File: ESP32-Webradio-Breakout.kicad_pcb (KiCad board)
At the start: 2 copper layers, 113.7 x 85.1 mm, 6 parts, among them J1 Conn_01x19, J2 Conn_01x19, SW1 RotaryEncoder_Switch

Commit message: adding RCA Jack Connector to board
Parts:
- added J3: RCJ-042, RCJ-042:CUI_RCJ-042, F.Cu at (212.9, 56.9)
- added J4: RCJ-041, RCJ-041:CUI_RCJ-041, F.Cu at (212.9, 71.2)

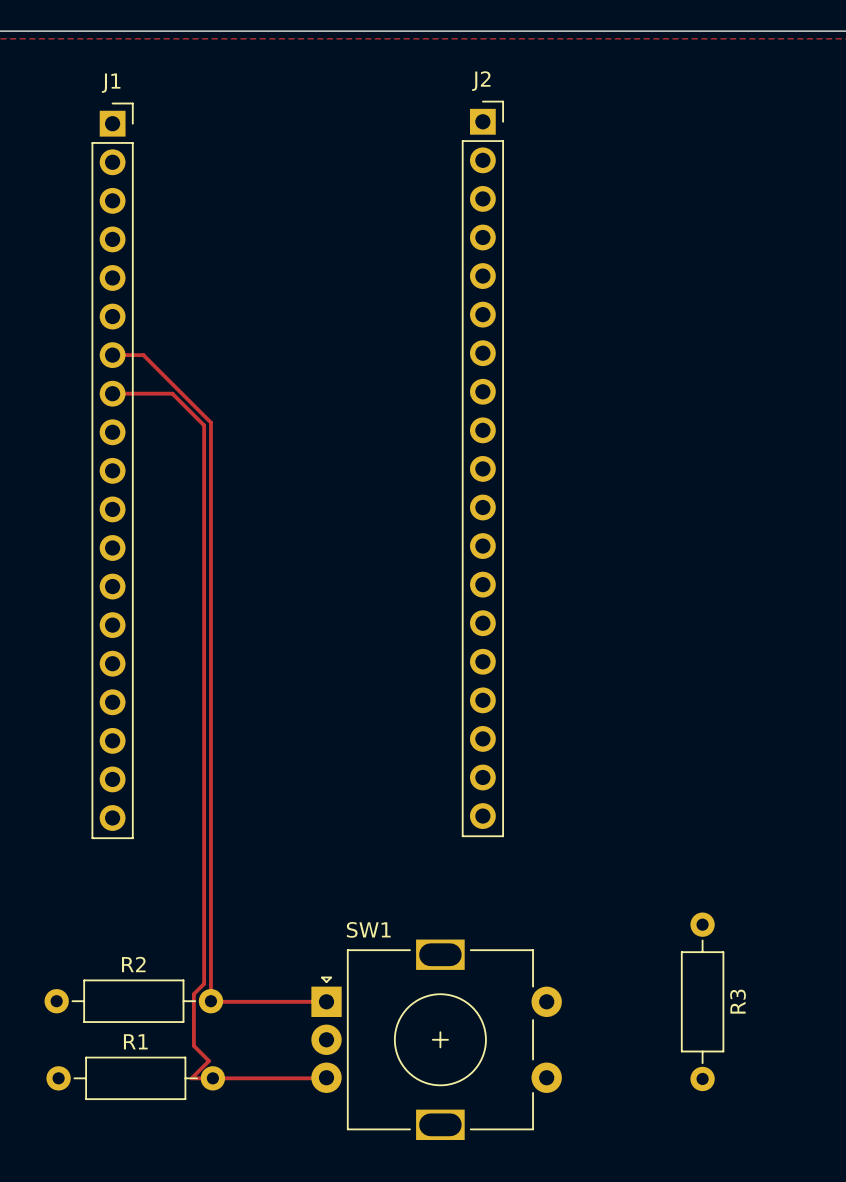
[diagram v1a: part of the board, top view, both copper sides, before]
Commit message: adding ESP32-NodeMCU to Project Lib
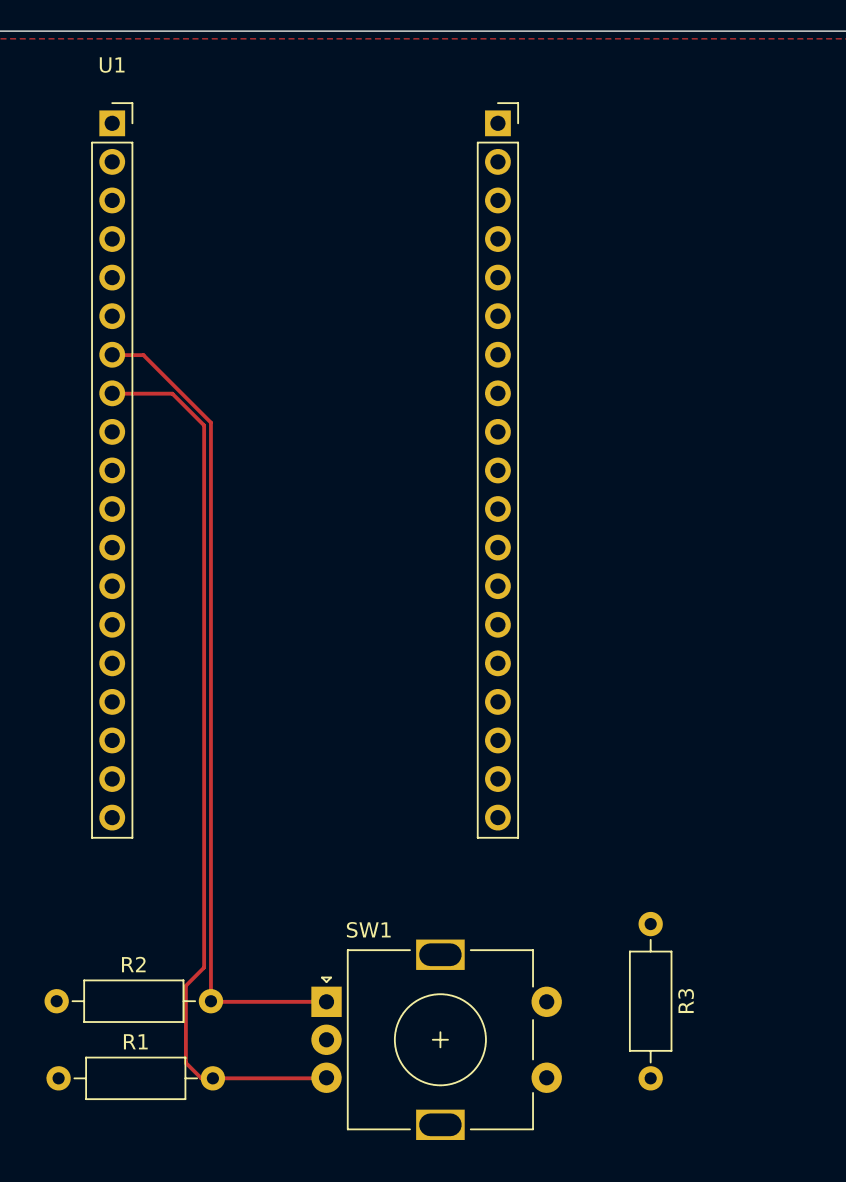
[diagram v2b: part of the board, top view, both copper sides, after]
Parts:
- removed J1, J2: Conn_01x19, Connector_PinSocket_2.54mm:PinSocket_1x19_P2.54mm_Vertical
- added U1: ESP32NodeMCU, ESP32-NodeMCU_WROOM_32:ESP32-NodeMCU_WROOM_32, F.Cu at (112.1, 43.0)
- moved R3 3.42 mm to (147.6, 95.8)
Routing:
- net /G33/Enc_B: track 59.9 -> 59.1 mm

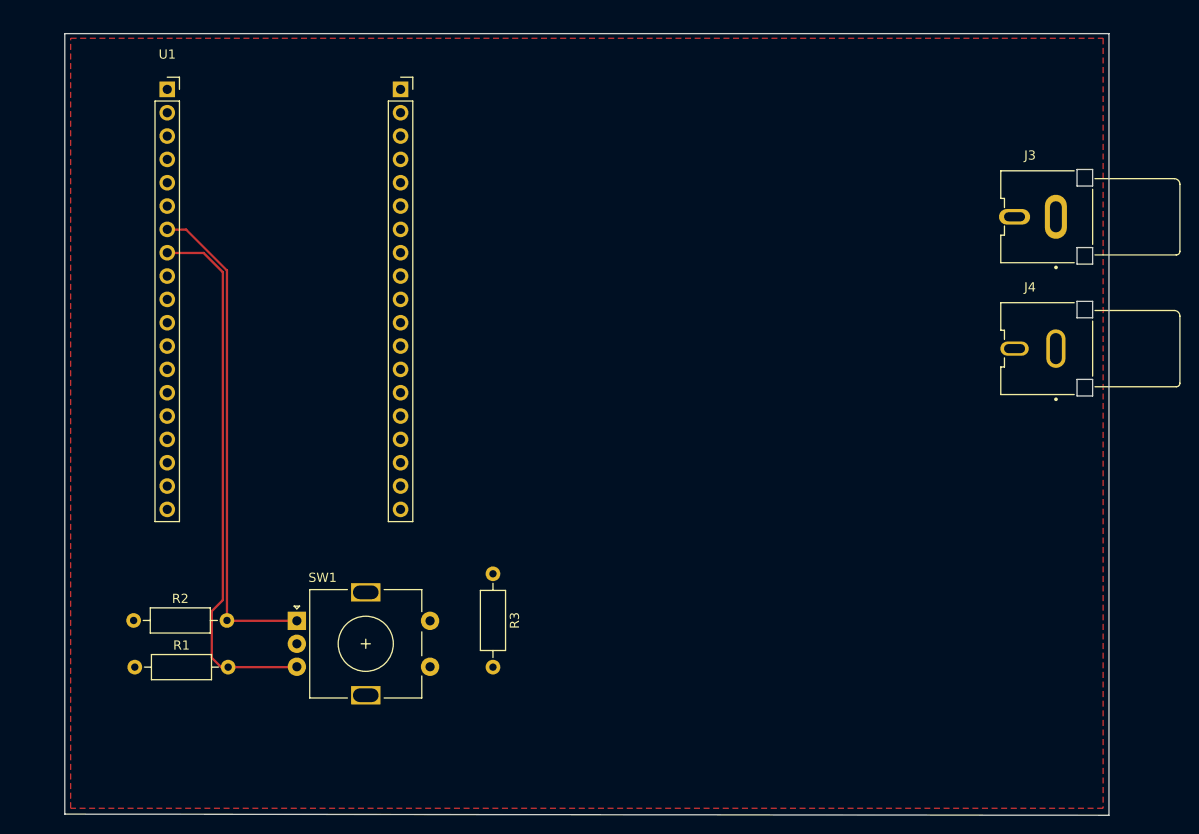
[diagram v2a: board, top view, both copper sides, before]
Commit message: adding CC BY-SA 4.0 licens to the Project
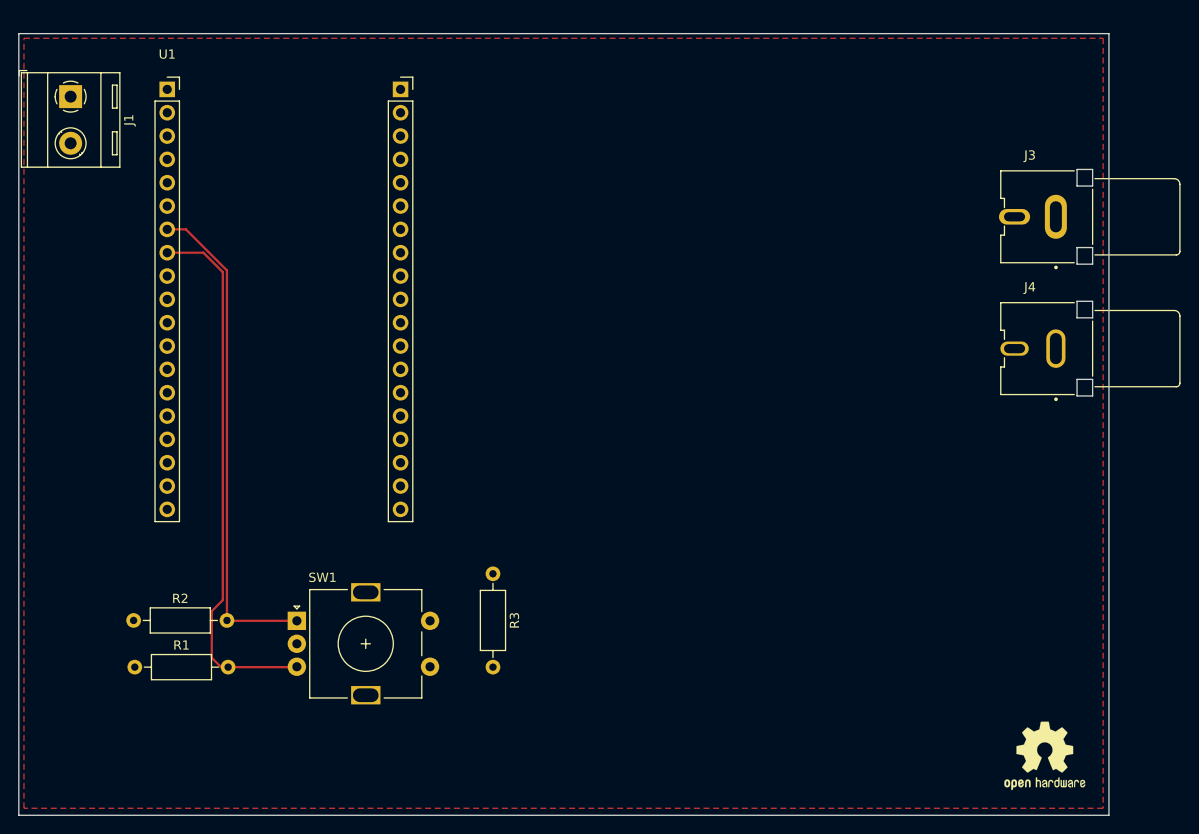
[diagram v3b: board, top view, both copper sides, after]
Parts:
- added J1: Conn_01x02, TerminalBlock_RND:TerminalBlock_RND_205-00287_1x02_P5.08mm_Horizontal, F.Cu at (101.6, 43.8)
- added REF**: OSHW-Logo2_9.8x8mm_SilkScreen, Symbol:OSHW-Logo2_9.8x8mm_SilkScreen, F.Cu at (207.6, 115.6)
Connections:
- U1 pad 32: unconnected-(U1-Pad32) -> GND
- U1 pad 38: unconnected-(U1-Pad38) -> GND
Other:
- board size 113.7 x 85.1 mm -> 118.7 x 85.1 mm

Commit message: adding some Power Supply components
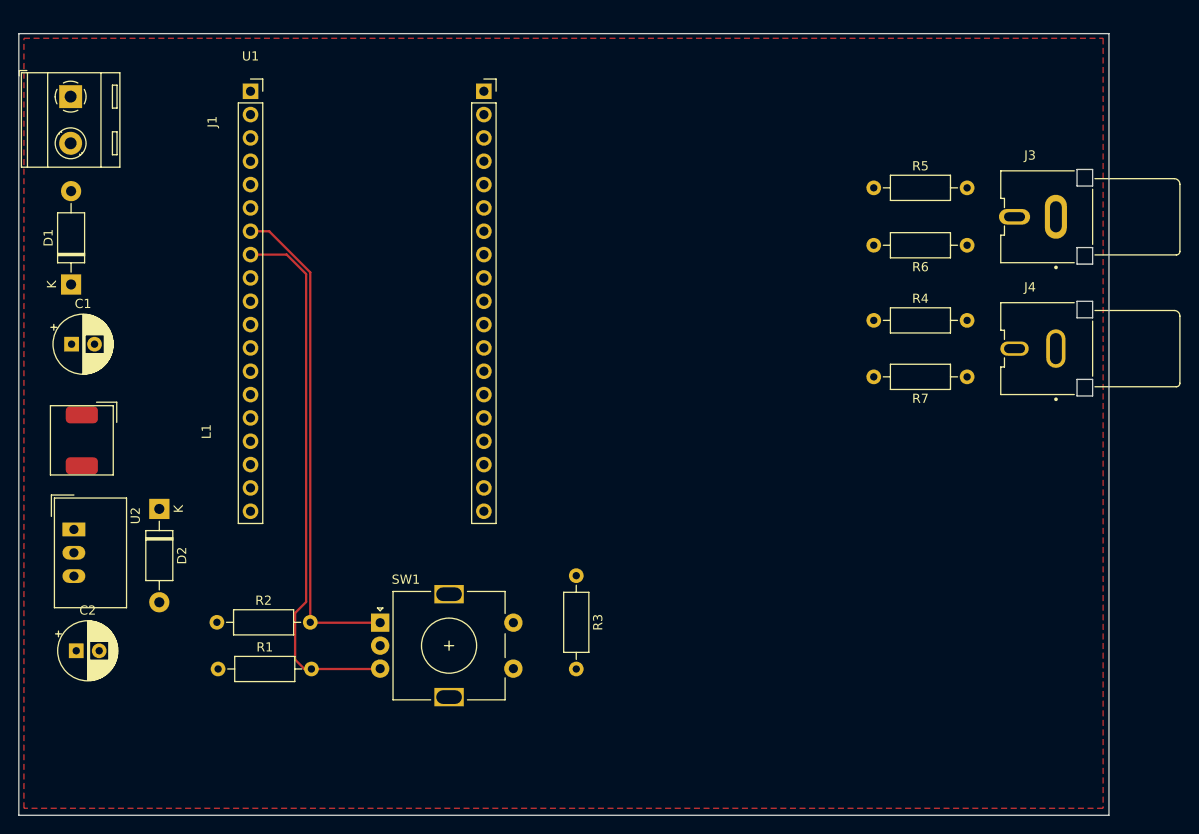
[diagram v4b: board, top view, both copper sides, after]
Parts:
- removed REF**: OSHW-Logo2_9.8x8mm_SilkScreen, Symbol:OSHW-Logo2_9.8x8mm_SilkScreen
- added C1: 4.7 uF/50V, Capacitor_THT:CP_Radial_D6.3mm_P2.50mm, F.Cu at (101.7, 70.8)
- added C2: 4.7 uF/50V, Capacitor_THT:CP_Radial_D6.3mm_P2.50mm, F.Cu at (102.2, 104.1)
- added D1: 1N4001, Diode_THT:D_DO-41_SOD81_P10.16mm_Horizontal, F.Cu at (101.7, 64.3)
- added D2: 1N4001, Diode_THT:D_DO-41_SOD81_P10.16mm_Horizontal, F.Cu at (111.3, 88.7)
- added L1: 8.2 uH/1.5 A/0.08 W, Inductor_SMD:L_AVX_LMLP07A7, F.Cu at (102.8, 81.2)
- added R4: 22k, Resistor_THT:R_Axial_DIN0207_L6.3mm_D2.5mm_P10.16mm_Horizontal, F.Cu at (189.0, 68.2)
- added R5: 22k, Resistor_THT:R_Axial_DIN0207_L6.3mm_D2.5mm_P10.16mm_Horizontal, F.Cu at (189.0, 53.7)
- added R6: 4k7, Resistor_THT:R_Axial_DIN0207_L6.3mm_D2.5mm_P10.16mm_Horizontal, F.Cu at (199.2, 60.0)
- added R7: 4k7, Resistor_THT:R_Axial_DIN0207_L6.3mm_D2.5mm_P10.16mm_Horizontal, F.Cu at (199.2, 74.3)
- added U2: TSR_1-2450, Converter_DCDC:Converter_DCDC_TRACO_TSR-1_THT, F.Cu at (102.0, 90.9)
- moved R1 9.07 mm to (117.7, 106.1)
- moved R2 9.07 mm to (117.5, 101.0)
- moved SW1 9.07 mm to (135.3, 101.1)
- moved U1 9.07 mm to (121.2, 43.2)
- moved R3 9.07 mm to (156.6, 96.0)
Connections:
- J1 pad 2: +3V3 -> Net-(J1-Pad2)
- J3 pad 1: unconnected-(J3-Pad1) -> Net-(J3-Pad1)
- J3 pad 2: unconnected-(J3-Pad2) -> GND
- J4 pad 1: unconnected-(J4-Pad1) -> Net-(J4-Pad1)
- J4 pad 2: unconnected-(J4-Pad2) -> GND
- U1 pad 10: unconnected-(U1-Pad10) -> /G26/Audio_L
- U1 pad 9: unconnected-(U1-Pad9) -> /G25/Audio_R

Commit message: Display and Remote 8-Bit I/O Expander for I2C added
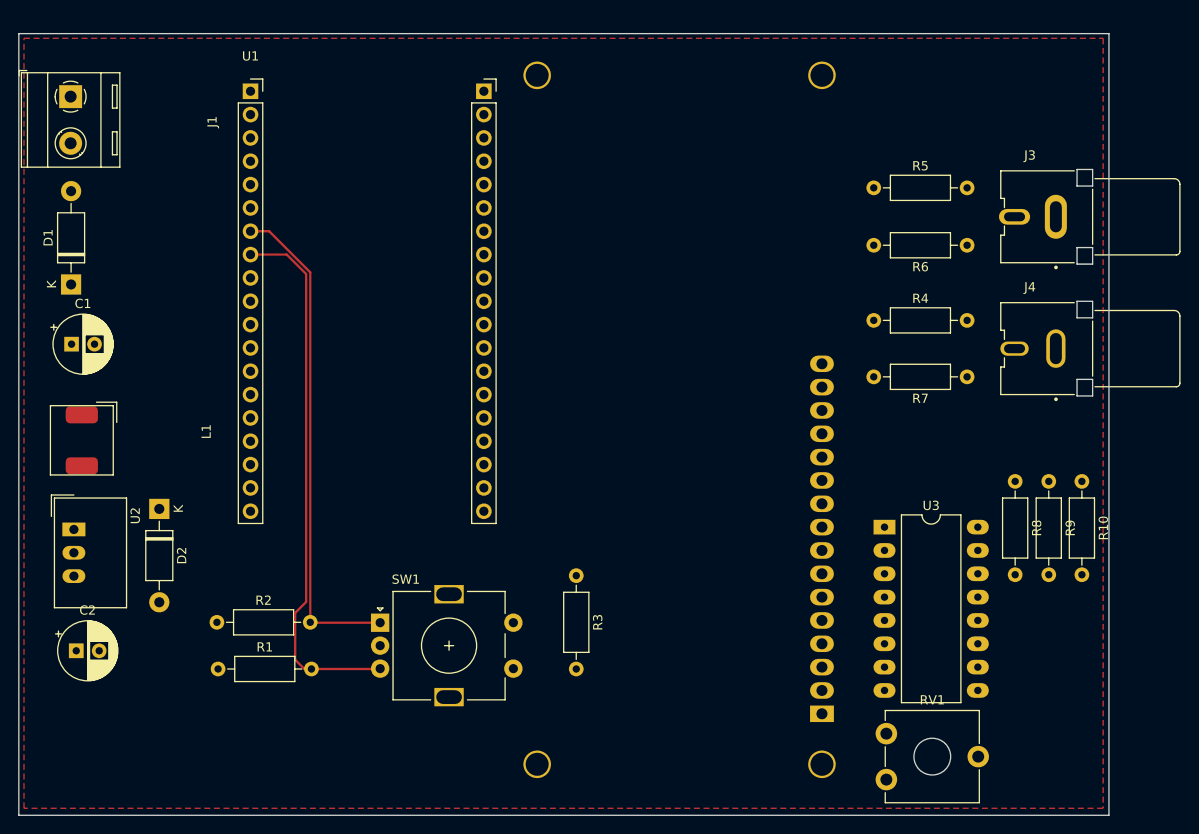
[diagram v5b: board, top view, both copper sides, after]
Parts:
- added DS1: WC1602A, Display:WC1602A, B.Cu at (183.4, 111.0)
- added R10: 10k, Resistor_THT:R_Axial_DIN0207_L6.3mm_D2.5mm_P10.16mm_Horizontal, F.Cu at (211.7, 85.7)
- added R8: 10k, Resistor_THT:R_Axial_DIN0207_L6.3mm_D2.5mm_P10.16mm_Horizontal, F.Cu at (204.4, 85.7)
- added R9: 10k, Resistor_THT:R_Axial_DIN0207_L6.3mm_D2.5mm_P10.16mm_Horizontal, F.Cu at (208.1, 85.7)
- added RV1: R_Potentiometer, Potentiometer_THT:Potentiometer_ACP_CA9-V10_Vertical_Hole, F.Cu at (190.4, 118.2)
- added U3: PCF8574, Package_DIP:DIP-16_W10.16mm_LongPads, F.Cu at (190.2, 90.7)

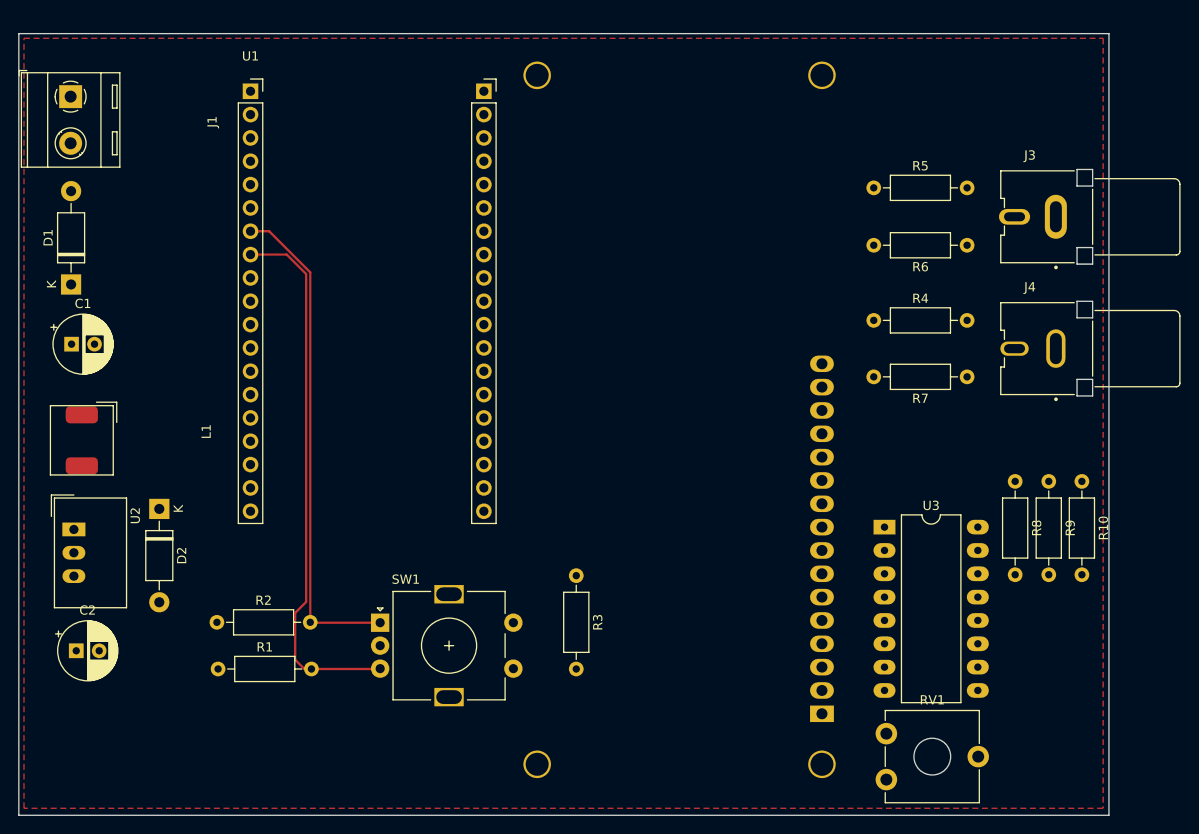
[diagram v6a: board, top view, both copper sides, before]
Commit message: Adding NPN-Transistor to switch the Backlight
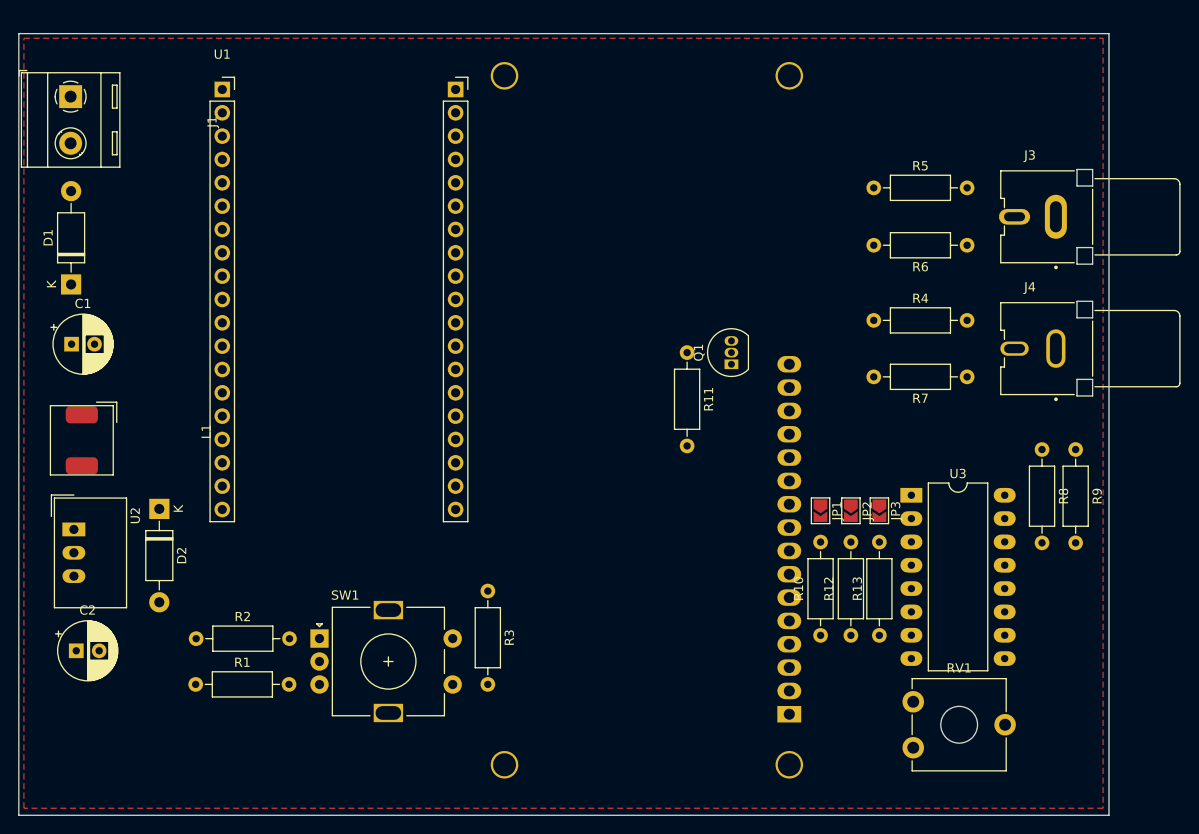
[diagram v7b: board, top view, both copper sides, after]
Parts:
- added JP1: SolderJumper_2_Open, Jumper:SolderJumper-2_P1.3mm_Open_TrianglePad1.0x1.5mm, F.Cu at (183.2, 88.9)
- added JP2: SolderJumper_2_Open, Jumper:SolderJumper-2_P1.3mm_Open_TrianglePad1.0x1.5mm, F.Cu at (186.5, 88.9)
- added JP3: SolderJumper_2_Open, Jumper:SolderJumper-2_P1.3mm_Open_TrianglePad1.0x1.5mm, F.Cu at (189.6, 88.9)
- added Q1: BC547, Package_TO_SOT_THT:TO-92_Inline, F.Cu at (173.5, 72.9)
- added R11: 4k7, Resistor_THT:R_Axial_DIN0207_L6.3mm_D2.5mm_P10.16mm_Horizontal, F.Cu at (168.7, 71.7)
- added R12: 10k, Resistor_THT:R_Axial_DIN0207_L6.3mm_D2.5mm_P10.16mm_Horizontal, F.Cu at (186.5, 102.5)
- added R13: 10k, Resistor_THT:R_Axial_DIN0207_L6.3mm_D2.5mm_P10.16mm_Horizontal, F.Cu at (189.6, 102.5)
- R8, R9: value 10k -> 4k7
- moved R10 33.0 mm to (183.2, 102.5), turned to 90 degrees
- moved R3 9.77 mm to (147.0, 97.6)
- moved SW1 6.83 mm to (128.7, 102.8)
- moved R8 4.54 mm to (207.3, 82.2)
- moved R9 4.54 mm to (211.0, 82.2)
- moved RV1 4.54 mm to (193.3, 114.7)
- moved U3 4.54 mm to (193.1, 87.2)
- moved DS1 3.56 mm to (179.8, 111.0)
- moved U1 3.08 mm to (118.1, 43.0)
- moved R1 2.96 mm to (115.2, 107.8)
- moved R2 2.88 mm to (115.3, 102.8)
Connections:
- DS1 pad 15: unconnected-(DS1-Pad15) -> +5V
- DS1 pad 16: GND -> Net-(DS1-Pad16)
- DS1 pad 4: Net-(U3-Pad6) -> /P0
- DS1 pad 6: Net-(U3-Pad4) -> /P2
- R10 pad 2: unconnected-(U3-Pad13) -> Net-(U3-Pad1)
- U3 pad 1: GND -> Net-(U3-Pad1)
- U3 pad 2: GND -> Net-(U3-Pad2)
- U3 pad 3: GND -> Net-(U3-Pad3)
- U3 pad 4: Net-(U3-Pad4) -> /P0
- U3 pad 6: Net-(U3-Pad6) -> /P2
- U3 pad 7: unconnected-(U3-Pad7) -> /P3
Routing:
- net /G33/Enc_B: track 59.1 -> 0.06 mm
- net /G32/Enc_A: track 54.1 -> 0.00 mm
